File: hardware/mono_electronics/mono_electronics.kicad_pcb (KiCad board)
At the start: 4 copper layers, 190 x 148 mm, 181 parts, among them SW1 KMR2, U1 ESP32-S3FN8, Y1 L327S400H11L

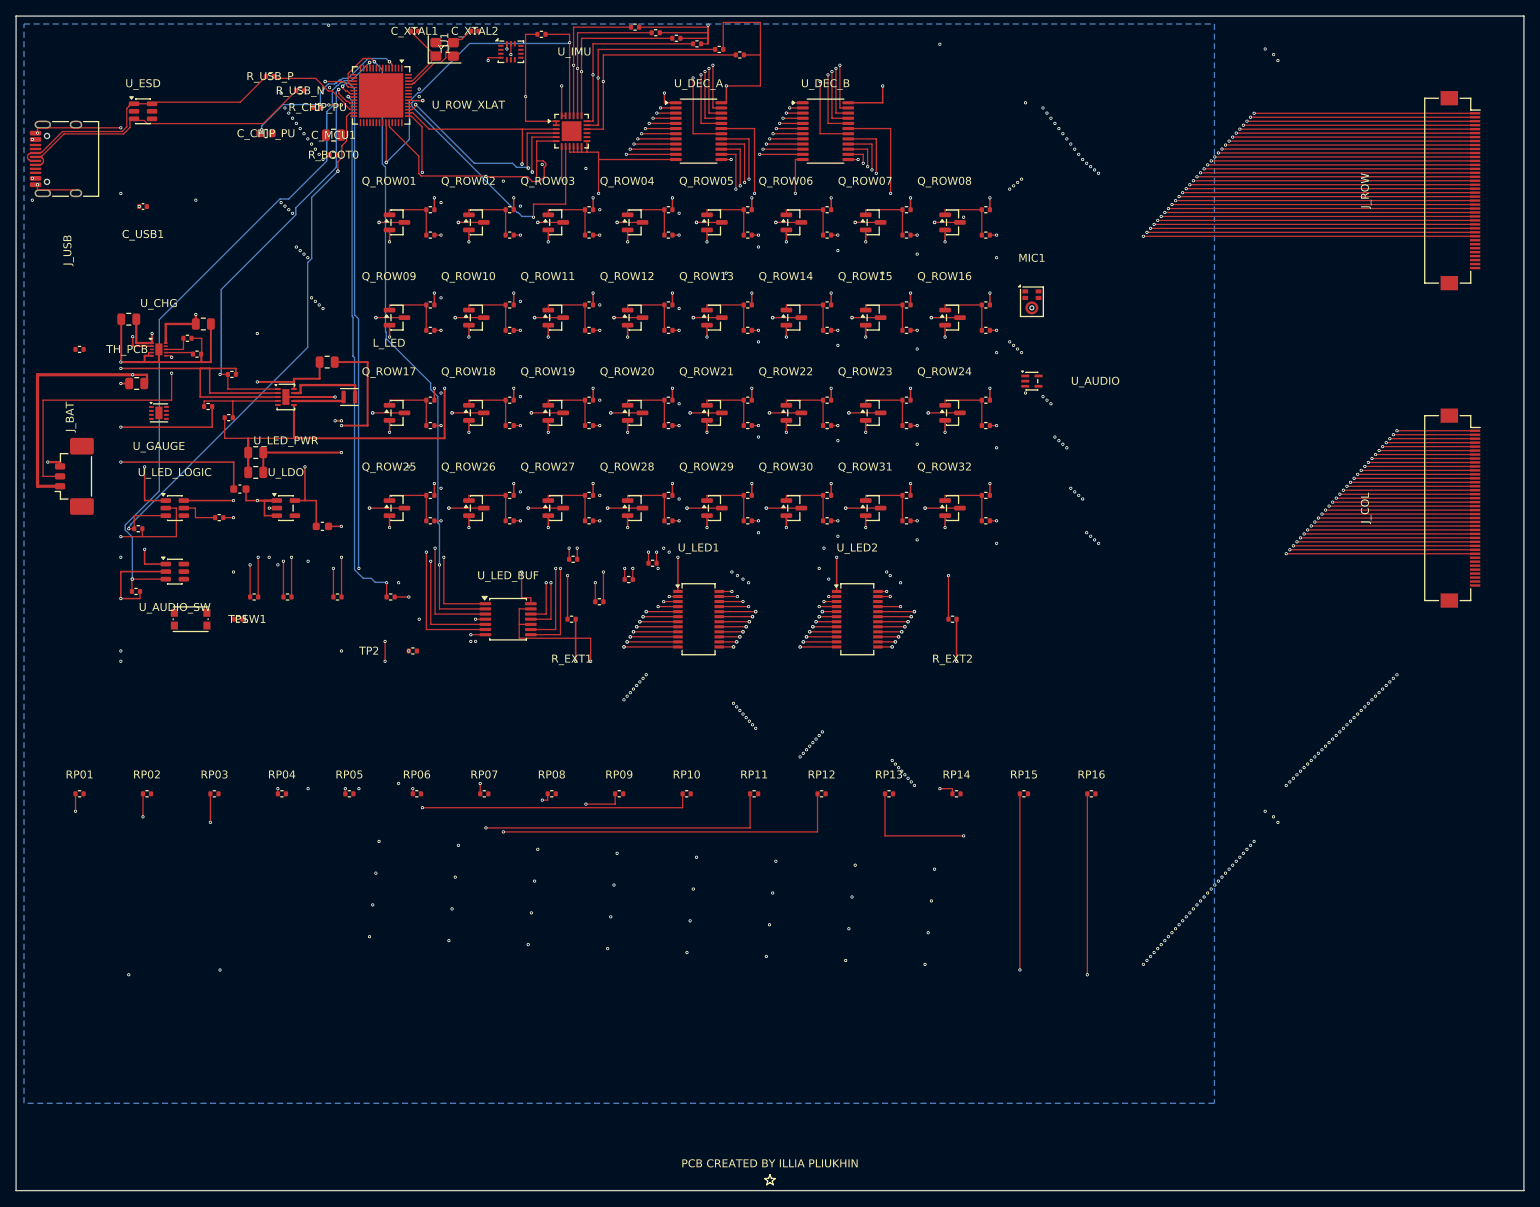
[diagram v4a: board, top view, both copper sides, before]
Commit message: MCU grid: DRC gate hard-fail, drc breakdown, post-grid helpers
Refuse to apply grid routes when neither engine passes 0-short/0-crossing gate.
Add drc_breakdown.py for unconnected-by-net reporting. Extend PathFinder prefer
pads for GPIO0_BOOT and USB_D_N_MCU; add In2-only AON/GND tie helpers (not enabled
by default — post-grid F/In2 routes still collide with applied grid). Document
remaining 39 unconnected groups in MONO_SPLIT_ARCHITECTURE.md.

Co-authored-by: illiapliukhin <illiapliukhin@users.noreply.github.com>
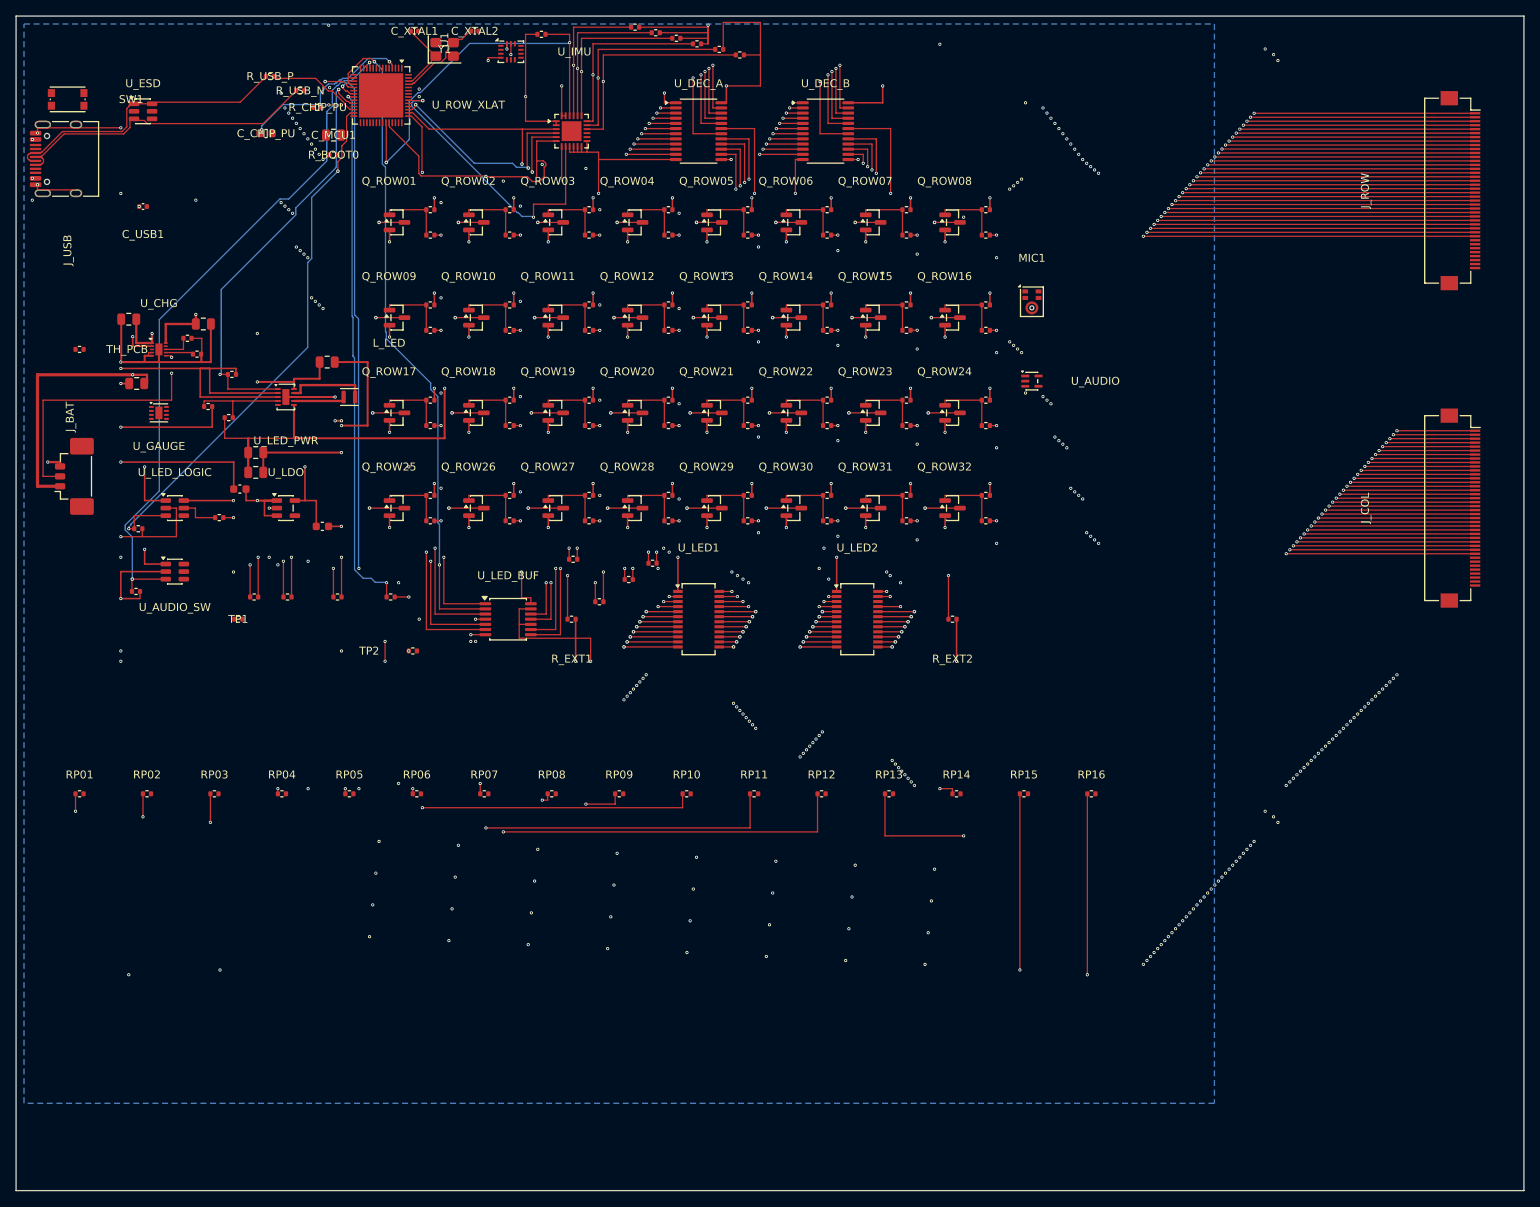
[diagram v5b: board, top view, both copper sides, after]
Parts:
- moved SW1 67.3 mm to (6.50, 10.5)
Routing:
- net AON_3V3: track 166.3 -> 167.4 mm

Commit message: Post-grid finish: GND pad vias, cleanup, incremental AON (0/0 gate)
Add mono_split_post_grid_finish.py with phased subprocess workflow: remove
dangling stubs, nudge ROW_XLAT_OE_N via for clearance, DRC-gated GND stitch
vias on F-only pads (via-in-pad), incremental AON north face, optional signals.
Pipeline defaults to cleanup,gnd,aon phases and restores backup if copper gate fails.

Co-authored-by: illiapliukhin <illiapliukhin@users.noreply.github.com>
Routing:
- net AON_3V3: track 167.4 -> 65.9 mm, vias 9 -> 6
- net ROW_A3: track 159.7 -> 64.3 mm, vias 2 -> 1
- net GND: track 915.7 -> 923.6 mm, vias 49 -> 59

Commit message: Fix dangling cleanup, dogbone GND, ROW rip-protect; DRC 0/0 unconnected 24
Co-authored-by: illiapliukhin <illiapliukhin@users.noreply.github.com>
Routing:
- net AON_3V3: track 65.9 -> 167.8 mm, vias 6 -> 9
- net ROW_A3: track 64.3 -> 158.9 mm, vias 1 -> 2
- net LED_CLK: track 140.4 -> 68.1 mm, vias 5 -> 4
- net GPIO0_BOOT: track 0.00 -> 56.8 mm, vias 0 -> 2
- net LED_SDI: track 136.8 -> 147.2 mm
- net ROW_A0: track 107.6 -> 112.3 mm, vias 3 -> 2
- net GND: track 923.6 -> 921.5 mm, vias 59 -> 62
- net CHIP_PU: track 21.6 -> 22.3 mm

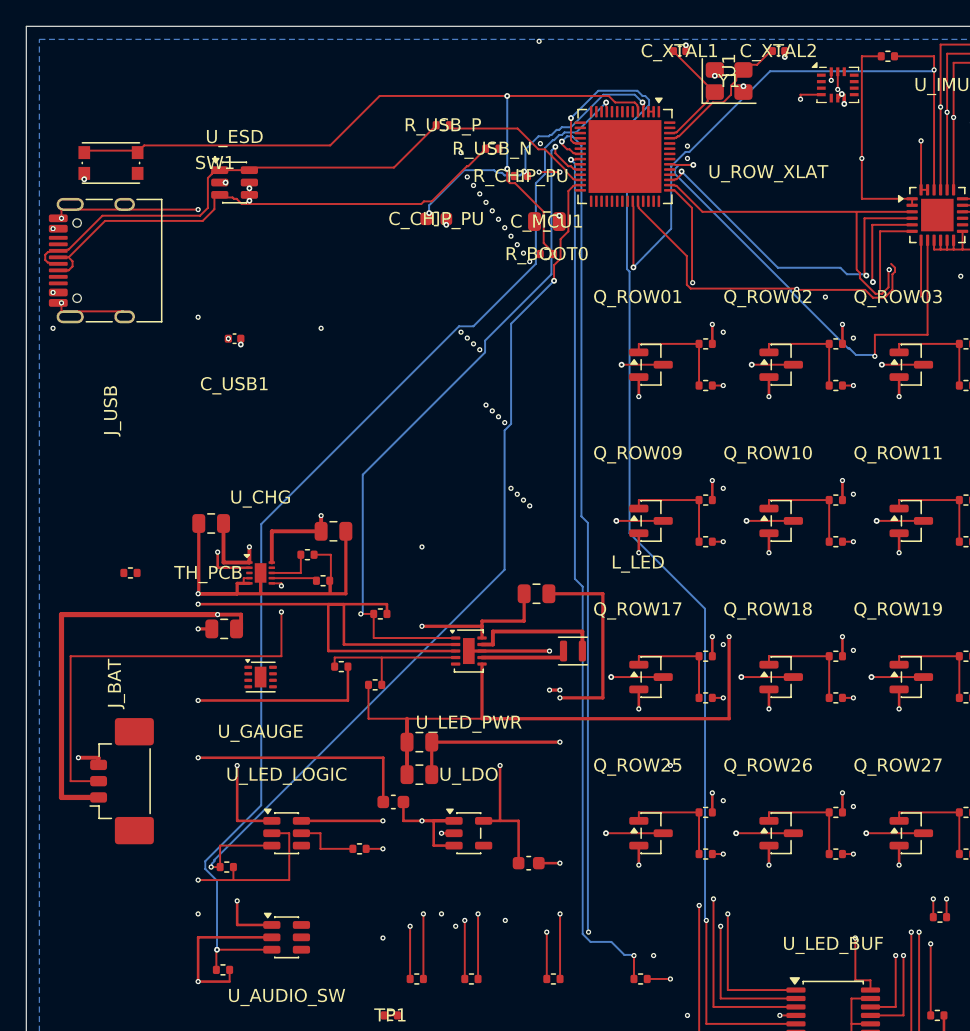
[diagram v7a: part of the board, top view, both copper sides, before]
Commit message: AON zone tuning, PF/greedy LED_CLK merge, idempotent gated apply
Co-authored-by: illiapliukhin <illiapliukhin@users.noreply.github.com>
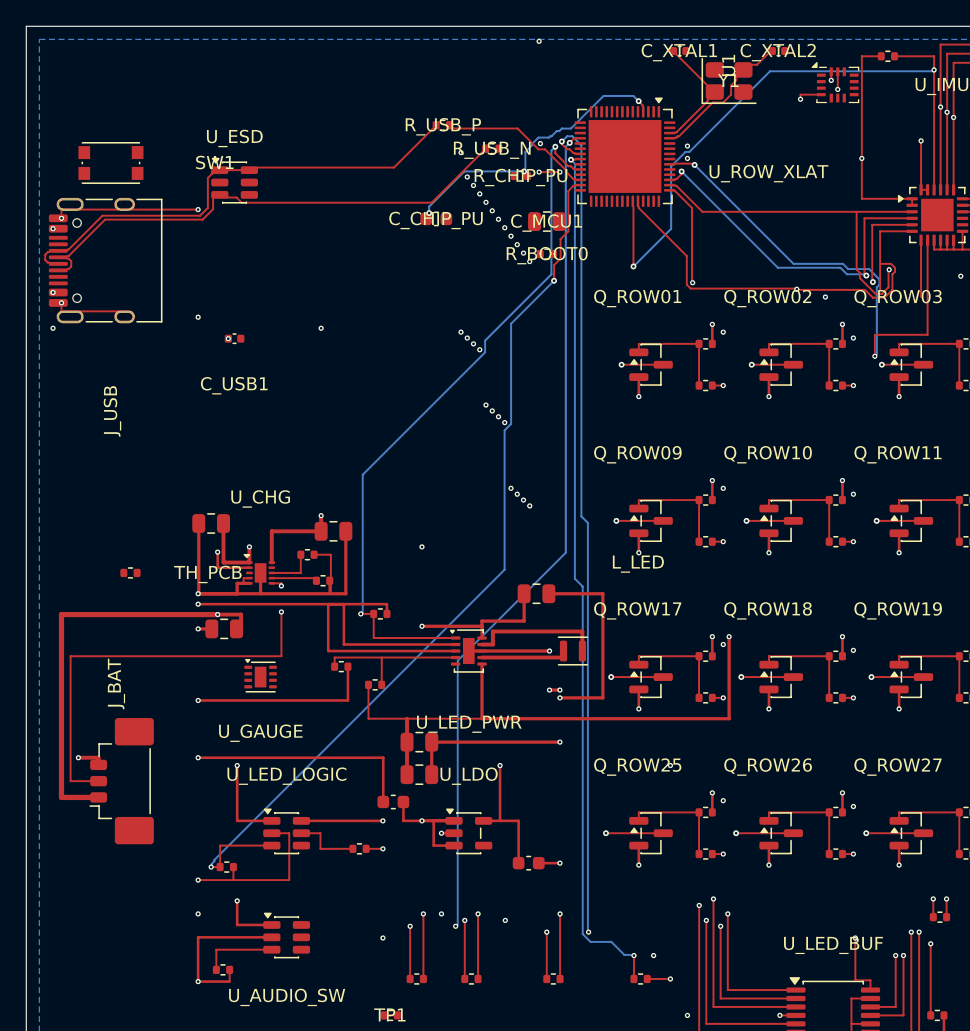
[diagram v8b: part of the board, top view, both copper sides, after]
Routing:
- net AUDIO_EN: track 85.7 -> 5.81 mm, vias 2 -> 0
- net LED_SDI: track 147.2 -> 71.9 mm, vias 6 -> 5
- net LED_CLK: track 68.1 -> 132.3 mm, vias 4 -> 5
- net GPIO0_BOOT: track 56.8 -> 0.00 mm, vias 2 -> 0
- net GND: track 921.5 -> 915.7 mm, vias 62 -> 49
- net DEC_B_EN_N: track 184.7 -> 185.6 mm
- net ROW_A3: track 158.9 -> 159.7 mm
- net CHIP_PU: track 22.3 -> 21.6 mm
